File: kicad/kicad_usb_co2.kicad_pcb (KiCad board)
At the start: 2 copper layers, 90 x 54 mm, 6 parts, among them SW1 SW_SPDT, SW2 SW_SPDT, U1 MH-Z19B, U2 SeeeduinoXIAO

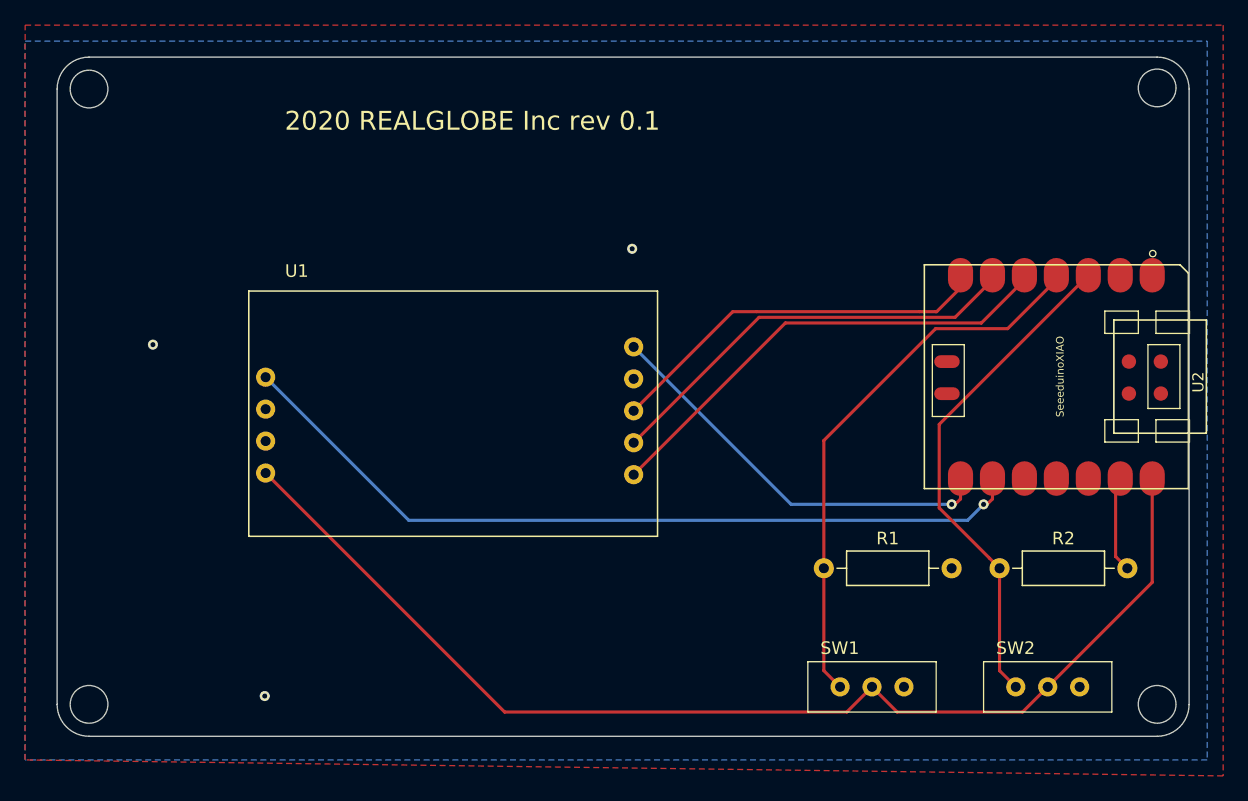
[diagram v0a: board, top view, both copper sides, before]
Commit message: kicadのフォルダをMH-Z14Aと19Bと共通にした
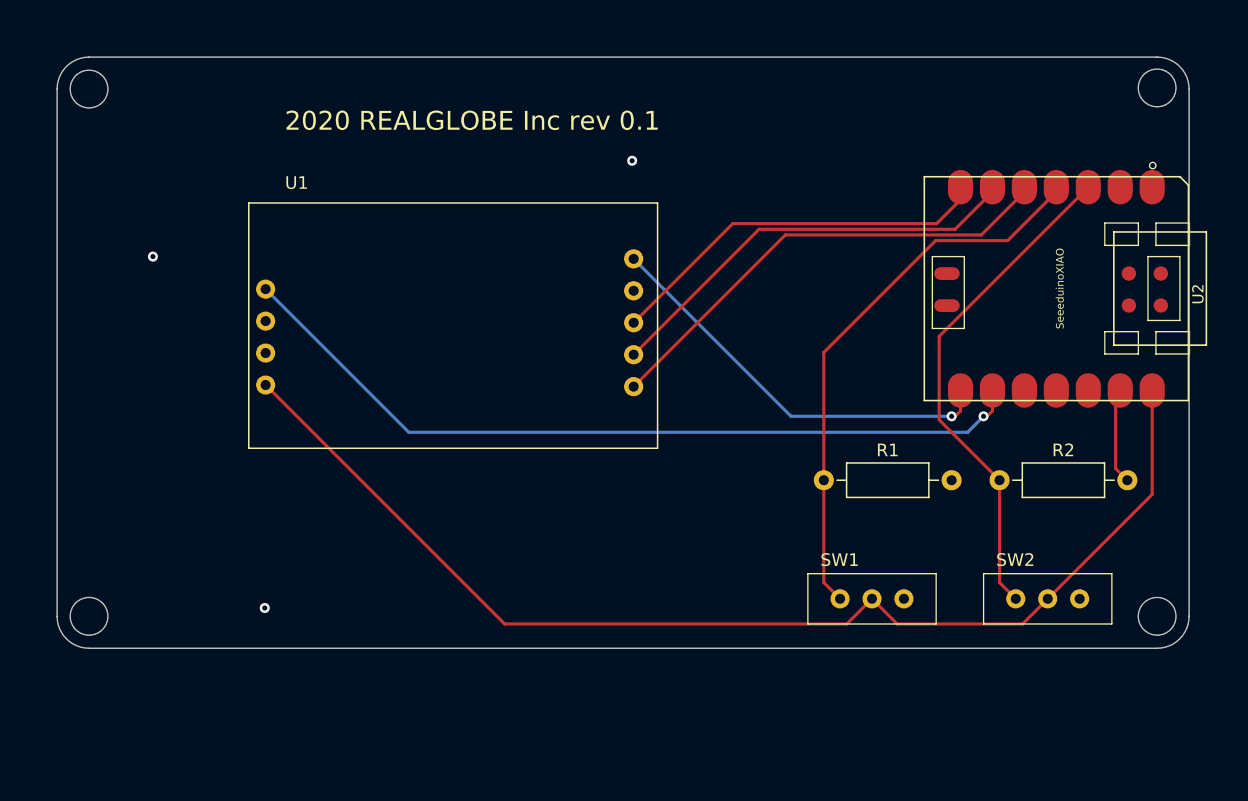
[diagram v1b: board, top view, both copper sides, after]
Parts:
- moved U2 7.00 mm to (69.0, 9.51)
- moved R1 7.00 mm to (61.0, 33.6)
- moved R2 7.00 mm to (74.9, 33.6)
- moved SW1 7.00 mm to (59.7, 45.1)
- moved SW2 7.00 mm to (73.7, 45.1)
- moved U1 7.00 mm to (15.2, 31.1)
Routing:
- removed copper zone on B.Cu, net GND
- removed copper zone on F.Cu, net GND
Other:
- board size 90 x 54 mm -> 90 x 47 mm

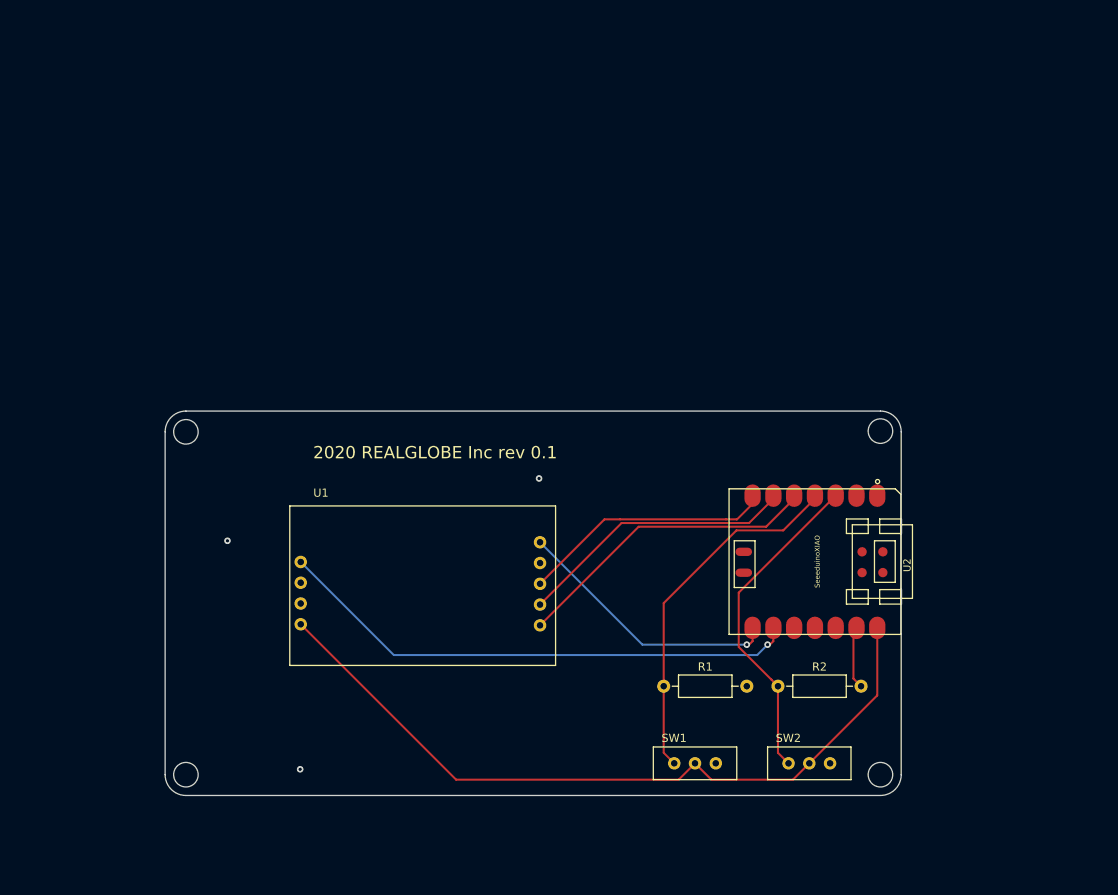
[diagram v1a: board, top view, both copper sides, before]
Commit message: 基板外形の修正と仮配置
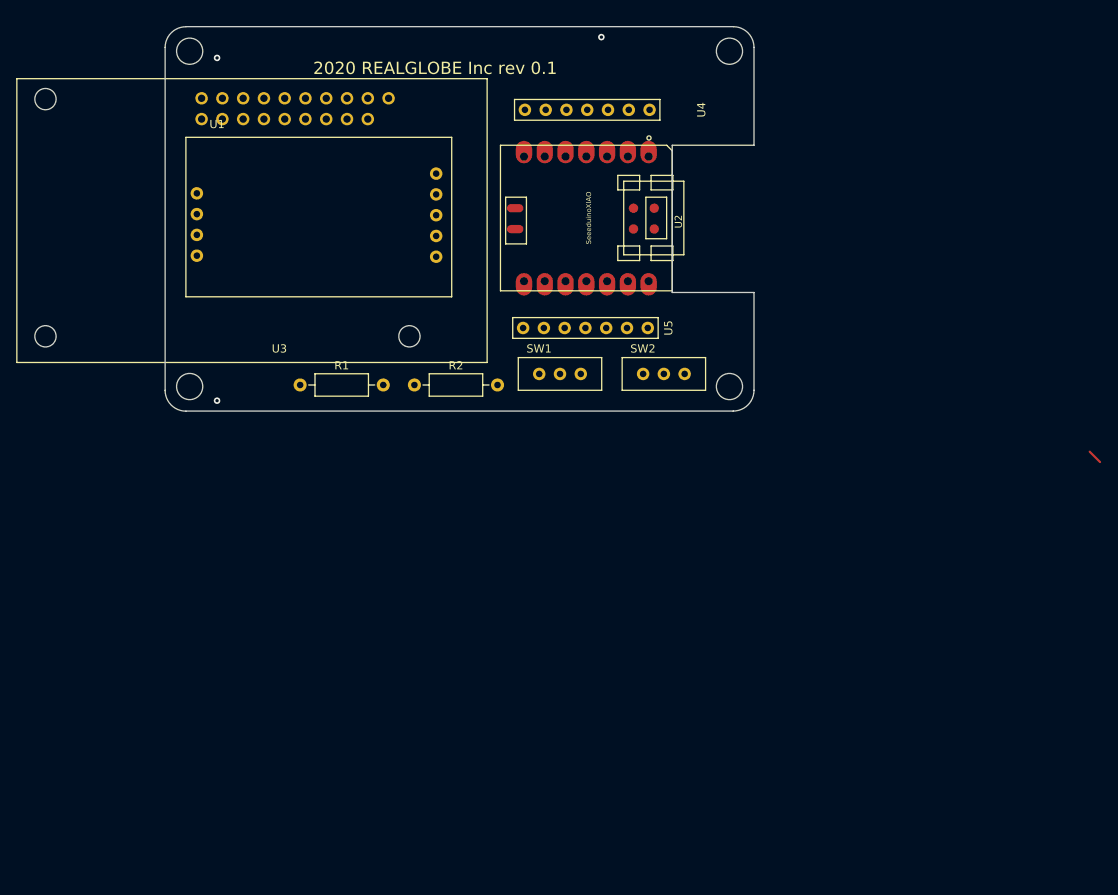
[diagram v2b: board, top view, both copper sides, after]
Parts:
- added U3: MH-Z14A, kicad_mylib:MH-Z14A, F.Cu at (39.4, -40.6)
- added U4: PinHeader_XIAO, kicad_mylib:PinHeader_XIAO, F.Cu at (60.5, -35.6)
- added U5: PinHeader_XIAO, kicad_mylib:PinHeader_XIAO, F.Cu at (42.5, -11.4)
- SW1, SW2: footprint Mylib:SW_SLIDE_sengoku -> kicad_mylib:SW_SLIDE_sengoku
- U1: footprint MH-Z19B:MH-Z19B -> kicad_mylib:MH-Z19B
- U2: footprint Seeeduino XIAO:Seeeduino XIAO-MOUDLE14P-2.54-21X17.8MM -> kicad_mylib:SeeedXIAO
- moved R1 57.7 mm to (16.5, -3.19)
- moved R2 57.7 mm to (30.5, -3.19)
- moved SW2 50.8 mm to (55.9, -2.54)
- moved U2 50.5 mm to (41.0, -32.5)
- moved SW1 50.4 mm to (43.2, -2.54)
- moved U1 46.8 mm to (2.54, -14.0)
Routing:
- net +5V: track 92.5 -> 0.00 mm
- net Net-(U1-Pad6): track 64.8 -> 0.00 mm, vias 1 -> 0
- net Net-(R1-Pad1): track 44.3 -> 1.82 mm
- net Net-(R2-Pad1): track 40.0 -> 0.00 mm
- net Net-(U1-Pad5): track 37.9 -> 0.00 mm
- net Net-(U1-Pad4): track 34.3 -> 0.00 mm
- net Net-(U1-Pad1): track 33.0 -> 0.00 mm, vias 1 -> 0
- net Net-(U1-Pad3): track 30.8 -> 0.00 mm
- net GND: track 7.52 -> 0.00 mm
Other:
- board size 90 x 47 mm -> 72 x 47 mm

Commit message: たぶん動く
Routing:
- net +5V: track 0.00 -> 128.9 mm
- net Net-(U1-Pad6): track 0.00 -> 68.9 mm
- net Net-(R1-Pad1): track 1.82 -> 65.6 mm
- net Net-(R2-Pad1): track 0.00 -> 62.8 mm
- net Net-(U1-Pad1): track 0.00 -> 56.0 mm
- net Net-(U1-Pad5): track 0.00 -> 55.8 mm
- net Net-(U1-Pad4): track 0.00 -> 42.5 mm
- net Net-(U1-Pad3): track 0.00 -> 35.3 mm
- net Net-(U2-Pad12): track 0.00 -> 4.94 mm
- net Net-(U2-Pad11): track 0.00 -> 4.94 mm
- net Net-(U2-Pad10): track 0.00 -> 4.94 mm
- net Net-(U2-Pad2): track 0.00 -> 4.93 mm
- net Net-(U2-Pad1): track 0.00 -> 4.93 mm
- added copper zone on B.Cu, net GND
- added copper zone on F.Cu, net GND

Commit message: シルクのリビジョンをインクリした
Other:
- board text added: "2020 REALGLOBE Inc rev 0.3"
- board text removed: "2020 REALGLOBE Inc rev 0.1"
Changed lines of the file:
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@@
   (gr_circle (center 3 -44) (end 4.6 -44) (layer Edge.Cuts) (width 0.05))
   (gr_arc (start 2.54 -44.45) (end 2.54 -46.99) (angle -90) (layer Edge.Cuts) (width 0.05))
-  (gr_text "2020 REALGLOBE Inc rev 0.1" (at 33.02 -41.91) (layer F.SilkS)
+  (gr_text "2020 REALGLOBE Inc rev 0.3" (at 33.02 -41.91) (layer F.SilkS)
     (effects (font (size 1.5 1.5) (thickness 0.3)))
   )
